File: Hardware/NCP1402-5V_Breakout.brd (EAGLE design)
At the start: 12.7 x 16.5 mm, 11 parts, among them U1 NCP1402

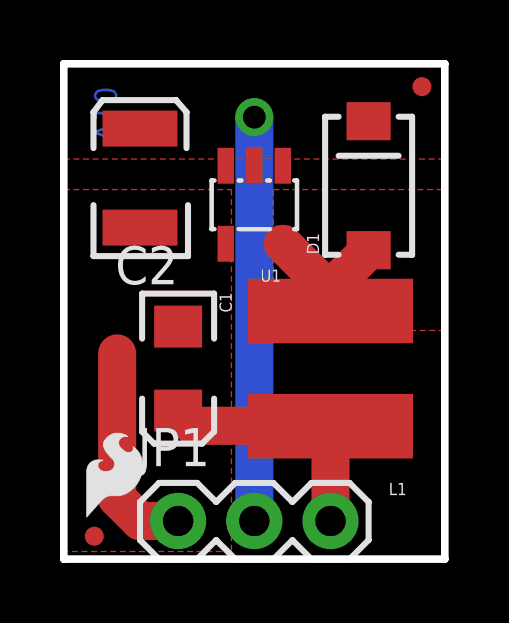
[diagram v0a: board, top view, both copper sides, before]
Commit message: changed fiducials to regular from micro
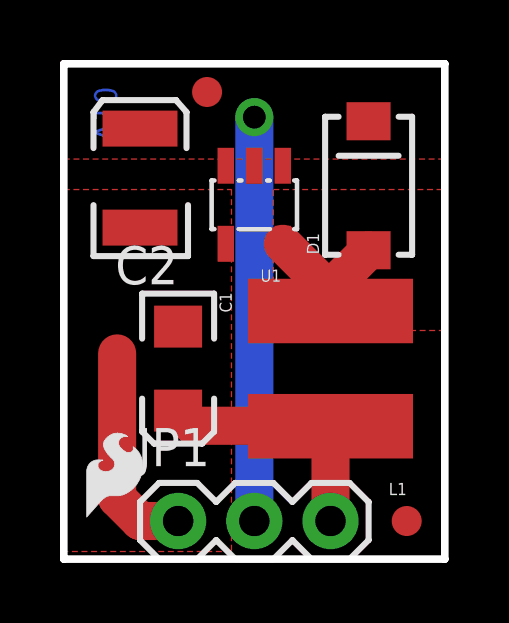
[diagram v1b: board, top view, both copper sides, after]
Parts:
- removed JP3, JP4: FIDUCIALUFIDUCIAL, SparkFun:MICRO-FIDUCIAL
- added FID1, FID2: FIDUCIAL1X2, SparkFun-Aesthetics:FIDUCIAL-1X2
